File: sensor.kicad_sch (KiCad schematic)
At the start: 2 parts, among them U2 ICM-42688-P

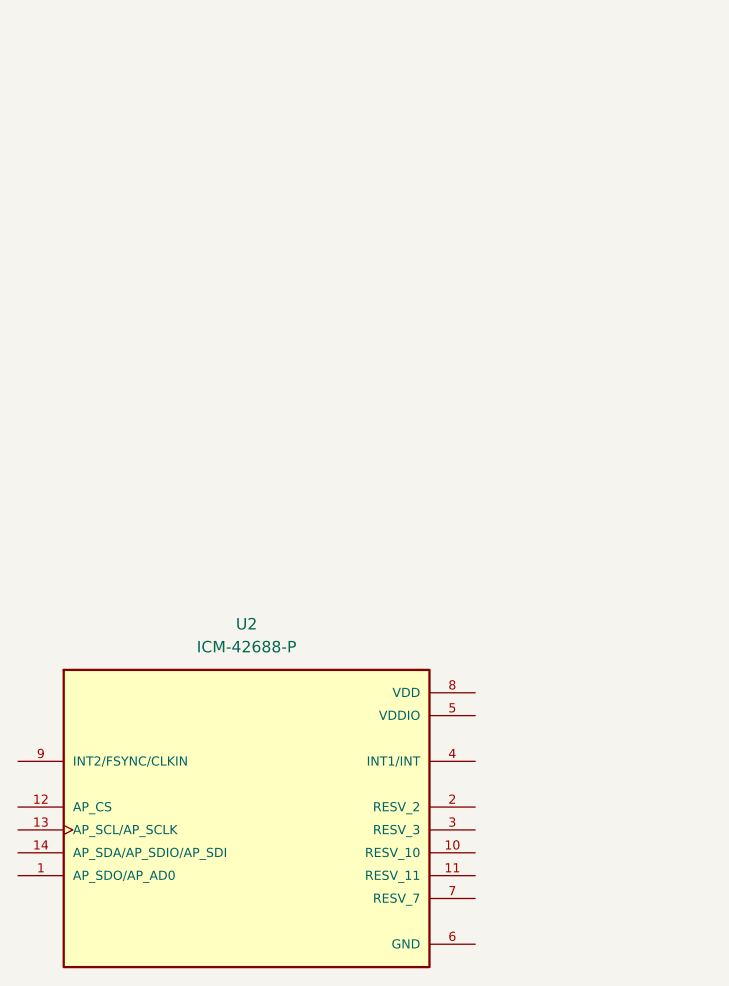
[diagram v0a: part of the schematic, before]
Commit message: Refactor sensor.kicad_sch: Adjust component positions and update property attributes for ICM-42688-P
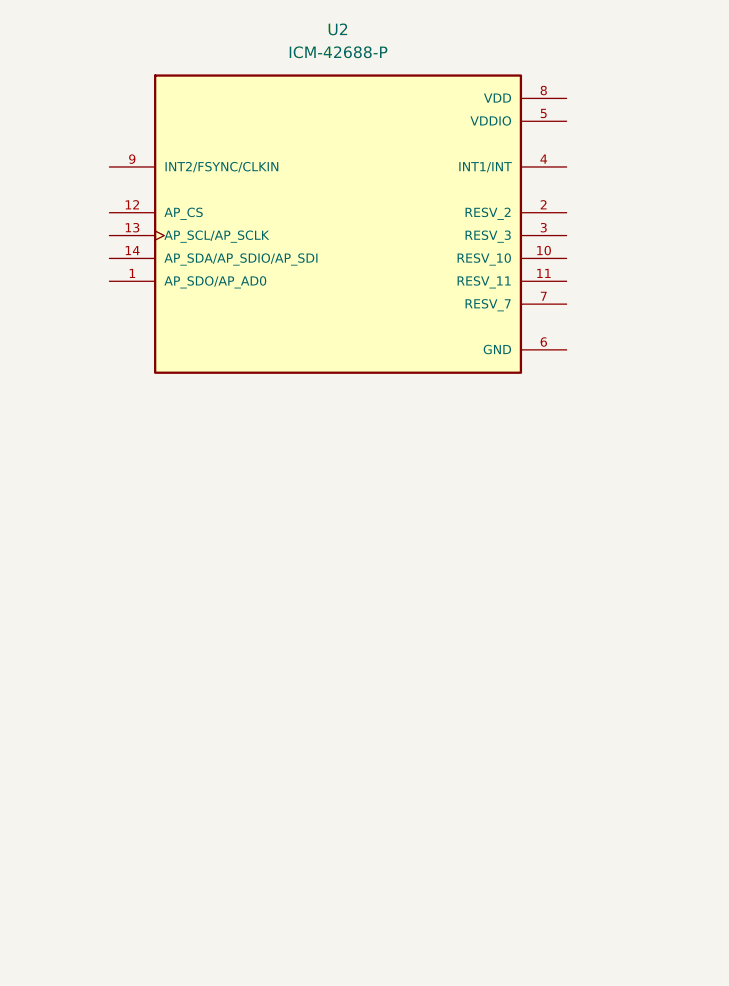
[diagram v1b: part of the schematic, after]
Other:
- moved on the sheet: U2
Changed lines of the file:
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@@
 	(symbol
 		(lib_id "fcg4:ICM-42688-P")
-		(at 68.58 116.84 0)
+		(at 78.74 50.8 0)
 		(unit 1)
 		(exclude_from_sim no)
@@
 		(fields_autoplaced yes)
 		(property "Reference" "U2"
-			(at 68.58 96.52 0)
+			(at 78.74 30.48 0)
 			(effects
 				(font
@@
 		)
 		(property "Value" "ICM-42688-P"
-			(at 68.58 99.06 0)
+			(at 78.74 33.02 0)
 			(effects
 				(font
@@
 		)
 		(property "Footprint" "fcg4_fp:PQFN50P300X250X97-14N"
-			(at 68.072 148.844 0)
+			(at 78.232 82.804 0)
 			(effects
 				(font
@@
 		)
 		(property "Datasheet" ""
-			(at 68.58 116.84 0)
+			(at 78.74 50.8 0)
 			(effects
 				(font
@@
 		)
 		(property "Description" ""
-			(at 68.58 116.84 0)
+			(at 78.74 50.8 0)
 			(effects
 				(font
@@
 		)
 		(property "DigiKey_Part_Number" "1428-ICM-42688-PCT-ND"
-			(at 68.58 98.298 0)
+			(at 78.74 32.258 0)
 			(effects
 				(font
@@
 		)
 		(property "SnapEDA_Link" "https://www.snapeda.com/parts/ICM-42688-P/TDK+InvenSense/view-part/?ref=snap"
-			(at 70.104 86.868 0)
+			(at 80.264 20.828 0)
 			(effects
 				(font
@@
 		)
 		(property "MAXIMUM_PACKAGE_HEIGHT" "0.97mm"
-			(at 68.834 82.296 0)
+			(at 78.994 16.256 0)
 			(effects
 				(font
@@
 		)
 		(property "Package" "LGA-14 TDK InvenSense"
-			(at 68.834 96.012 0)
+			(at 78.994 29.972 0)
 			(effects
 				(font
@@
 		)
 		(property "Check_prices" "https://www.snapeda.com/parts/ICM-42688-P/TDK+InvenSense/view-part/?ref=eda"
-			(at 68.834 92.964 0)
+			(at 78.994 26.924 0)
 			(effects
 				(font
@@
 		)
 		(property "STANDARD" "IPC-7351B"
-			(at 69.85 153.416 0)
+			(at 80.01 87.376 0)
 			(effects
 				(font
@@
 		)
 		(property "PARTREV" "1.2"
-			(at 69.342 75.438 0)
+			(at 79.502 9.398 0)
 			(effects
 				(font
@@
 		)
 		(property "MF" "TDK InvenSense"
-			(at 70.358 79.248 0)
+			(at 80.518 13.208 0)
 			(effects
 				(font
@@
 		)
 		(property "MP" "ICM-42688-P"
-			(at 68.58 144.526 0)
+			(at 78.74 78.486 0)
 			(effects
 				(font
@@
 		)
 		(property "Description_1" "Accelerometer, Gyroscope, 6 Axis Sensor - Output"
-			(at 69.342 141.224 0)
+			(at 79.502 75.184 0)
 			(effects
 				(font
@@
 		)
 		(property "MANUFACTURER" "TDK InvenSense"
-			(at 69.85 84.328 0)
+			(at 80.01 18.288 0)
 			(effects
 				(font

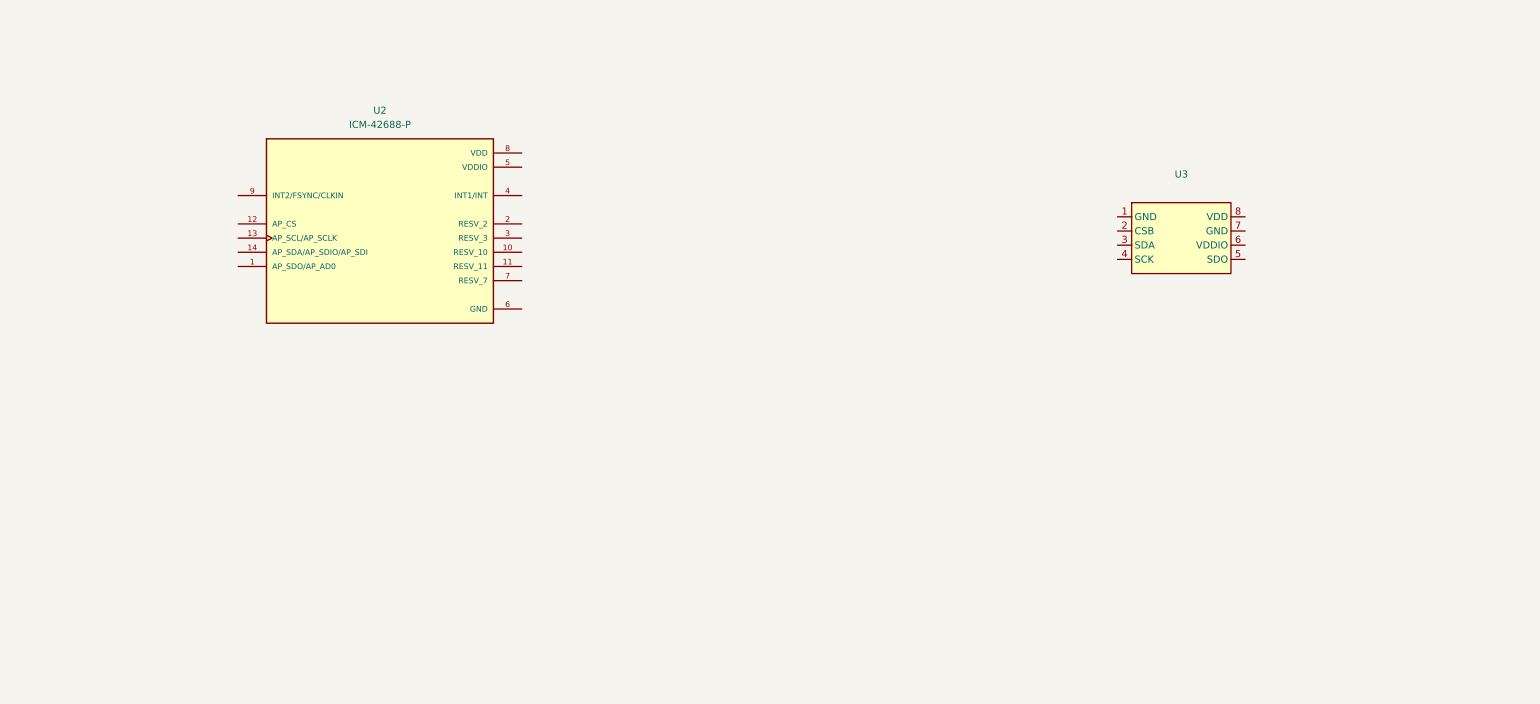
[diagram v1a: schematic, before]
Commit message: add sensors schematic
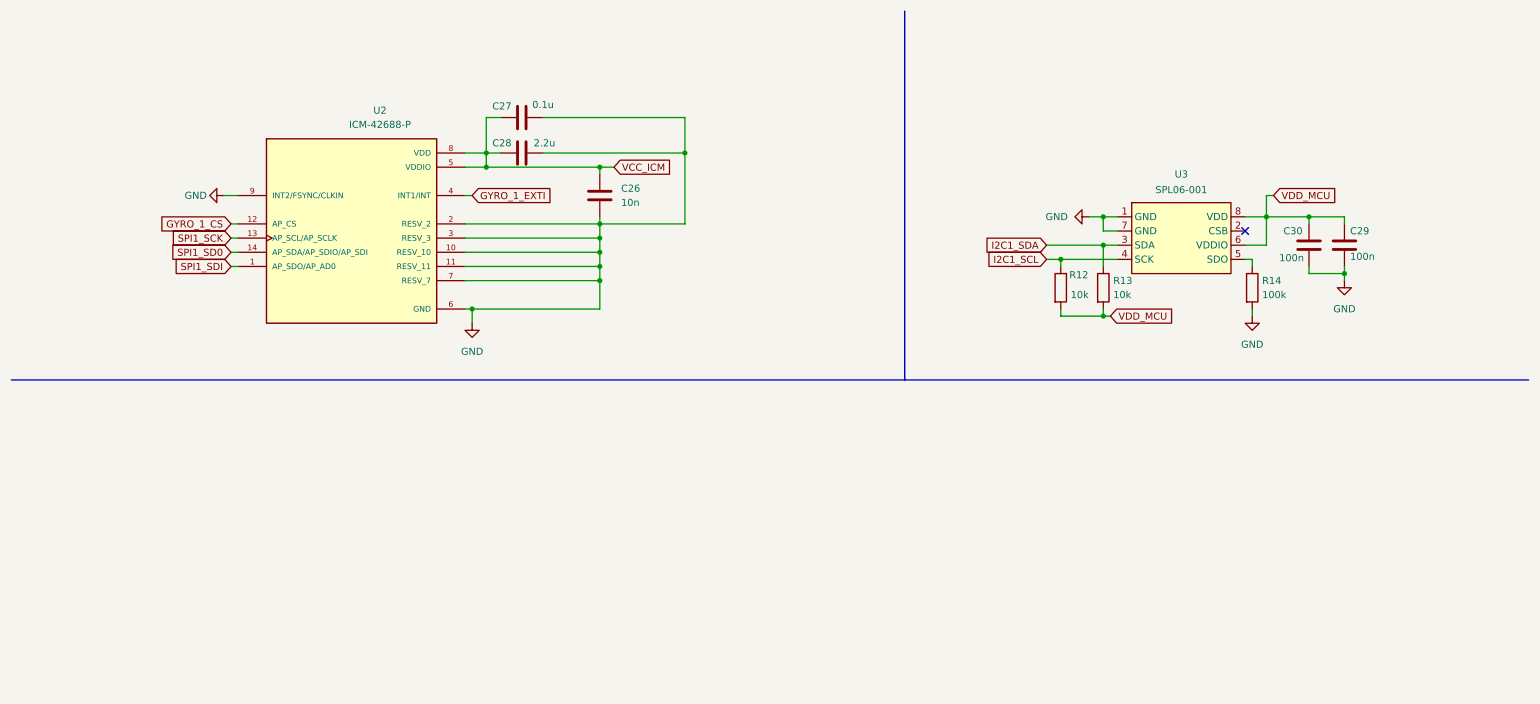
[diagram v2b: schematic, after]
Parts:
- added C26: 10n, symbol Device:C
- added C27: 0.1u, symbol Device:C
- added C28: 2.2u, symbol Device:C
- added C29, C30: 100n, symbol Device:C
- added R12, R13: 10k, symbol Device:R
- added R14: 100k, symbol Device:R
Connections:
- net SPI1_SDI: now reaches U2.1 (AP_SDO/AP_AD0)
- net GND: now reaches U2.10 (RESV_10)
- net GND: now also U2.11 (RESV_11), U2.2 (RESV_2), U2.3 (RESV_3), U2.6 (GND), U2.7 (RESV_7), U2.9 (INT2/FSYNC/CLKIN), U3.1 (GND), U3.7 (GND), C26.2, C27.2, C28.2, C29.1, C30.1, R14.2
- net GYRO_1_CS: now reaches U2.12 (AP_CS)
- net SPI1_SCK: now reaches U2.13 (AP_SCL/AP_SCLK)
- net SPI1_SD0: now reaches U2.14 (AP_SDA/AP_SDIO/AP_SDI)
- net GYRO_1_EXTI: now reaches U2.4 (INT1/INT)
- net VCC_ICM: now reaches U2.5 (VDDIO)
- net VCC_ICM: now also U2.8 (VDD), C26.1, C27.1, C28.1
- net I2C1_SDA: now reaches U3.3 (SDA)
- net I2C1_SDA: now also R13.1
- net I2C1_SCL: now reaches U3.4 (SCK)
- net I2C1_SCL: now also R12.1
- net at U3.5 (SDO): now also R14.1
- net VDD_MCU: now reaches U3.6 (VDDIO)
- net VDD_MCU: now also U3.8 (VDD), C29.2, C30.2, R12.2, R13.2
- no-connect marks 0 -> 1
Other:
- moved on the sheet: U2

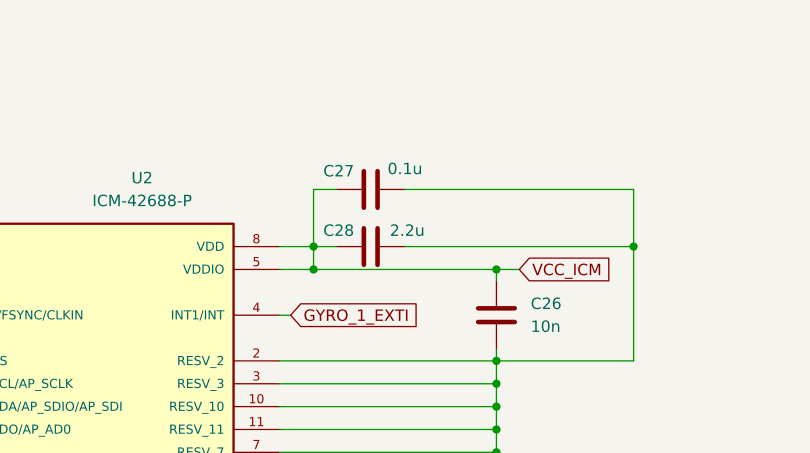
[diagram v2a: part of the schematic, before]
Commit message: - affected footprints for components - started placing components
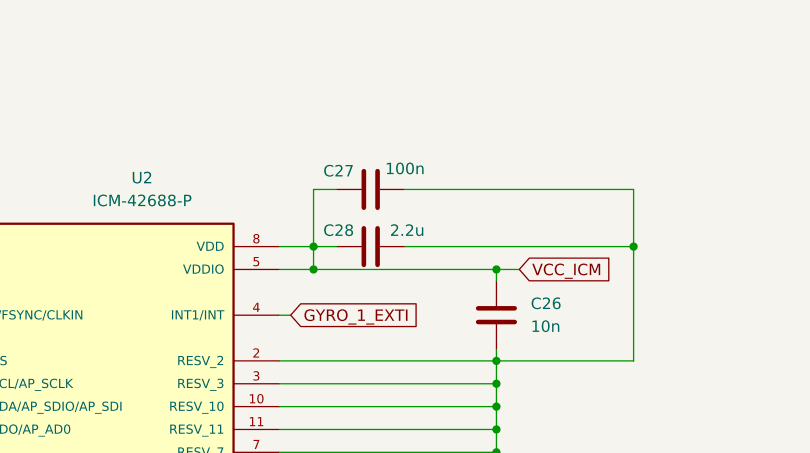
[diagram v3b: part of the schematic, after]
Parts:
- C26, C28, C29, C30: footprint (none) -> Capacitor_SMD:C_0402_1005Metric
- C27: value 0.1u -> 100n; footprint (none) -> Capacitor_SMD:C_0402_1005Metric
- R12, R13, R14: footprint (none) -> Resistor_SMD:R_0402_1005Metric
- U3: footprint ProLib_pcs_2026-02-12:SENSOR-SMD_SPL06-001 -> fcg4_fp:SENSOR-SMD_SPL06-001
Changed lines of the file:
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@@
 			)
 		)
-		(property "Footprint" ""
+		(property "Footprint" "Resistor_SMD:R_0402_1005Metric"
 			(at 206.502 62.23 90)
 			(effects
@@
 			)
 		)
-		(property "Footprint" ""
+		(property "Footprint" "Resistor_SMD:R_0402_1005Metric"
 			(at 198.882 62.23 90)
 			(effects
@@
 			)
 		)
-		(property "Value" "0.1u"
+		(property "Value" "100n"
 			(at 107.95 29.464 90)
 			(effects
@@
 			)
 		)
-		(property "Footprint" ""
+		(property "Footprint" "Capacitor_SMD:C_0402_1005Metric"
 			(at 107.95 30.7848 0)
 			(effects
@@
 			)
 		)
-		(property "Footprint" ""
+		(property "Footprint" "Resistor_SMD:R_0402_1005Metric"
 			(at 233.172 62.23 90)
 			(effects
@@
 			)
 		)
-		(property "Footprint" ""
+		(property "Footprint" "Capacitor_SMD:C_0402_1005Metric"
 			(at 107.95 37.1348 0)
 			(effects
@@
 			)
 		)
-		(property "Footprint" ""
+		(property "Footprint" "Capacitor_SMD:C_0402_1005Metric"
 			(at 250.4948 50.8 0)
 			(effects
@@
 			)
 		)
-		(property "Footprint" ""
+		(property "Footprint" "Capacitor_SMD:C_0402_1005Metric"
 			(at 119.0752 49.53 0)
 			(effects
@@
 			)
 		)
-		(property "Footprint" "ProLib_pcs_2026-02-12:SENSOR-SMD_SPL06-001"
+		(property "Footprint" "fcg4_fp:SENSOR-SMD_SPL06-001"
 			(at 222.25 42.164 0)
 			(effects
@@
 			)
 		)
-		(property "Footprint" ""
+		(property "Footprint" "Capacitor_SMD:C_0402_1005Metric"
 			(at 244.1448 50.8 0)
 			(effects

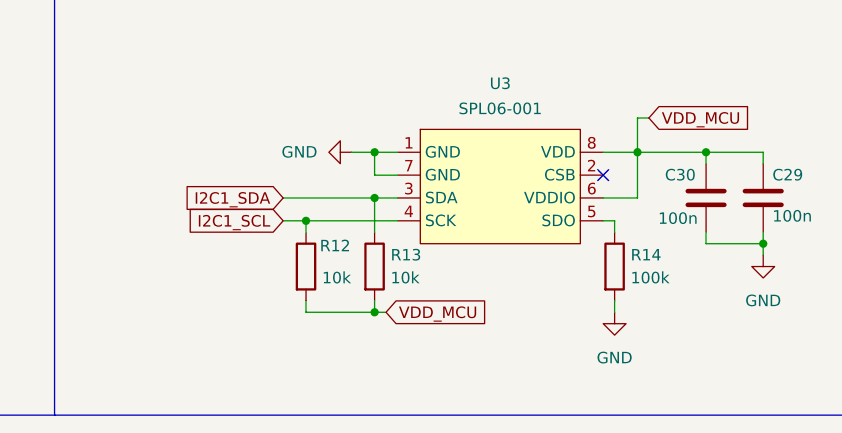
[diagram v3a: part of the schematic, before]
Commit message: Placed every components on one face only
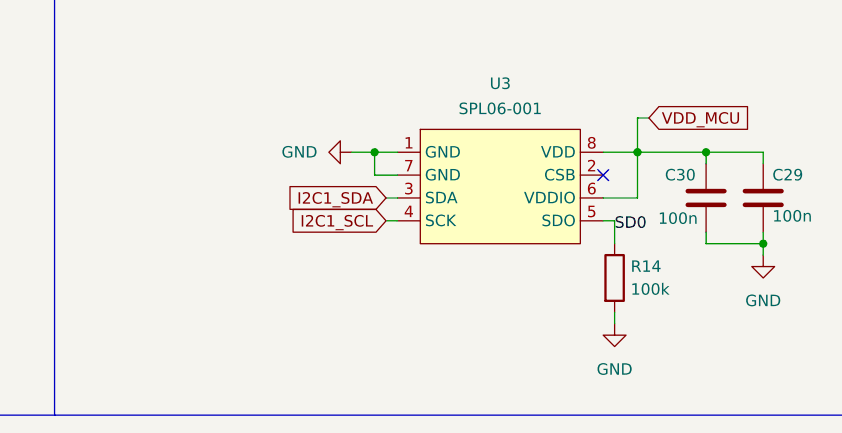
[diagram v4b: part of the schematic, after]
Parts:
- removed R12, R13: 10k, Resistor_SMD:R_0402_1005Metric, symbol Device:R
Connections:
- net SD0: now reaches R14.1, U3.5 (SDO)
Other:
- moved on the sheet: R14

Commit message: Update component properties in schematics with manufacturer details and datasheets
- Added manufacturer name, part number, and LCSC part name for various components in mcu.kicad_sch, power.kicad_sch, and sensor.kicad_sch.
- Updated datasheet links for components to point to the correct URLs.
- Ensured all new properties are hidden in the schematic view.
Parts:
- C27, C29, C30: LCSC Part Name (none) -> C77020; Manufacturer_Name (none) -> muRata; Manufacturer_Part_Number (none) -> GRM155R71H104KE14D
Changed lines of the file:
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@@
 			)
 		)
-		(property "Datasheet" "~"
+		(property "Datasheet" "https://www.lcsc.com/datasheet/C77020.pdf"
 			(at 104.14 31.75 0)
 			(effects
@@
 		(property "Description" "Unpolarized capacitor"
 			(at 104.14 31.75 0)
+			(effects
+				(font
+					(size 1.27 1.27)
+				)
+				(hide yes)
+			)
+		)
+		(property "LCSC Part Name" "C77020"
+			(at 104.14 31.75 90)
+			(effects
+				(font
+					(size 1.27 1.27)
+				)
+				(hide yes)
+			)
+		)
+		(property "Manufacturer_Name" "muRata"
+			(at 104.14 31.75 90)
+			(effects
+				(font
+					(size 1.27 1.27)
+				)
+				(hide yes)
+			)
+		)
+		(property "Manufacturer_Part_Number" "GRM155R71H104KE14D"
+			(at 104.14 31.75 90)
 			(effects
 				(font
@@
 			)
 		)
-		(property "Datasheet" "~"
+		(property "Datasheet" "https://www.lcsc.com/datasheet/C77020.pdf"
 			(at 251.46 54.61 0)
 			(effects
@@
 		)
 		(property "Description" "Unpolarized capacitor"
+			(at 251.46 54.61 0)
+			(effects
+				(font
+					(size 1.27 1.27)
+				)
+				(hide yes)
+			)
+		)
+		(property "LCSC Part Name" "C77020"
+			(at 251.46 54.61 0)
+			(effects
+				(font
+					(size 1.27 1.27)
+				)
+				(hide yes)
+			)
+		)
+		(property "Manufacturer_Name" "muRata"
+			(at 251.46 54.61 0)
+			(effects
+				(font
+					(size 1.27 1.27)
+				)
+				(hide yes)
+			)
+		)
+		(property "Manufacturer_Part_Number" "GRM155R71H104KE14D"
 			(at 251.46 54.61 0)
 			(effects
@@
 			)
 		)
-		(property "Datasheet" "~"
+		(property "Datasheet" "https://www.lcsc.com/datasheet/C77020.pdf"
 			(at 245.11 54.61 0)
 			(effects
@@
 			(at 245.11 54.61 0)
 			(effects
+				(font
+					(size 1.27 1.27)
+				)
+				(hide yes)
+			)
+		)
+		(property "LCSC Part Name" "C77020"
+			(at 245.11 54.61 0)
+			(effects
+				(font
+					(size 1.27 1.27)
+				)
+				(hide yes)
+			)
+		)
+		(property "Manufacturer_Name" "muRata"
+			(at 245.11 54.61 0)
+			(effects
+				(font
+					(size 1.27 1.27)
+				)
+				(hide yes)
+			)
+		)
+		(property "Manufacturer_Part_Number" "GRM155R71H104KE14D"
+			(at 245.11 54.61 0)
+			(effects
